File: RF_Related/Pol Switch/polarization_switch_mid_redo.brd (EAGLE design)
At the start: 88.4 x 54.4 mm, 61 parts, among them IC1 VLPR-24-858-2, IC10 ADP-2-1+_MINICIRCUITS, IC11 ADP-2-1+_MINICIRCUITS, IC12 QCV-151+, IC13 MAX8878EUK28+T, IC14 SN74LVC2G17DBVT, IC15 SN74LVC2G17DBVT, IC2 VLPR-24-858-2, IC3 HSWA2-30DR+, IC4 VLPR-24-858-2, IC5 HSWA2-30DR+, IC6 HSWA2-30DR+, IC7 HSWA2-30DR+, IC8 PHA-13LN+, IC9 PHA-13LN+, J1 M20-9730645, J2 171856-0002, X3 SMA-142-0701-801/806, X4 SMA-142-0701-801/806, X5 SMA-142-0701-801/806

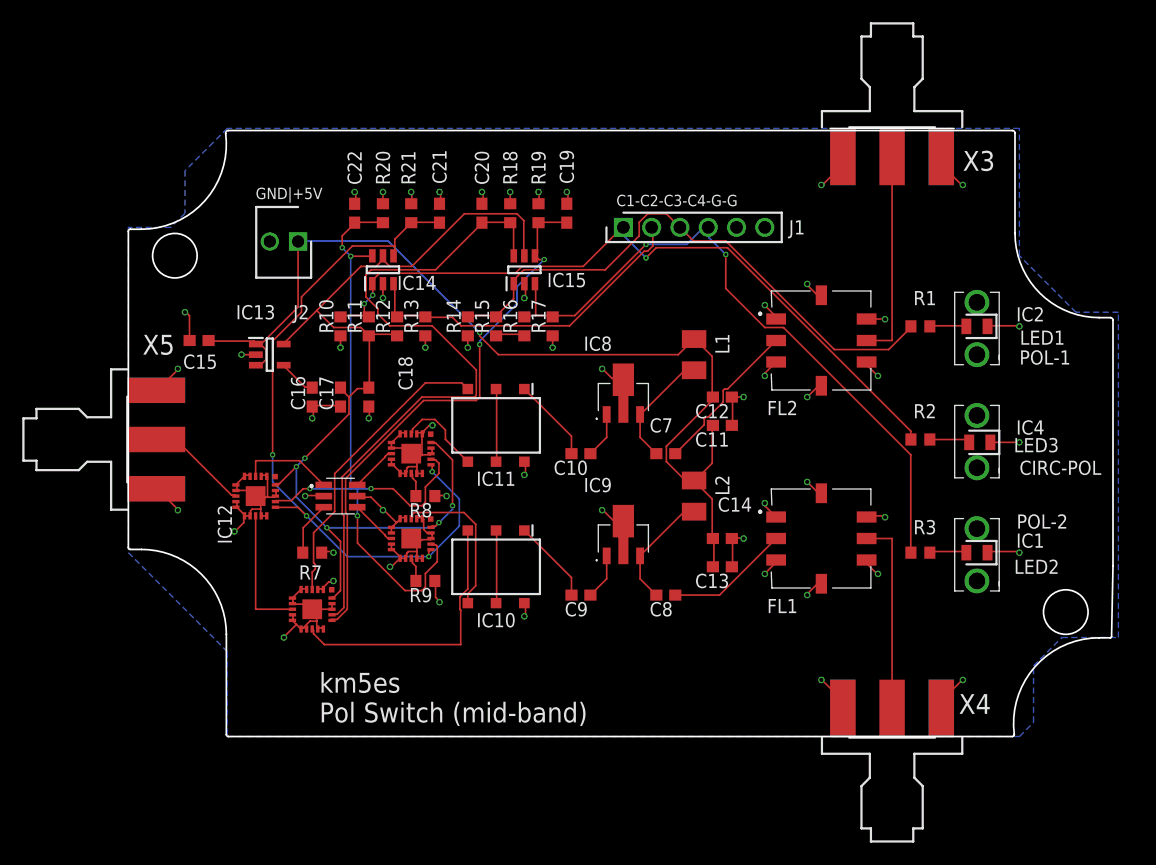
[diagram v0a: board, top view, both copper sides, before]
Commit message: made a new pol switch board with jumper pads. do I need that resistor row? backing up now
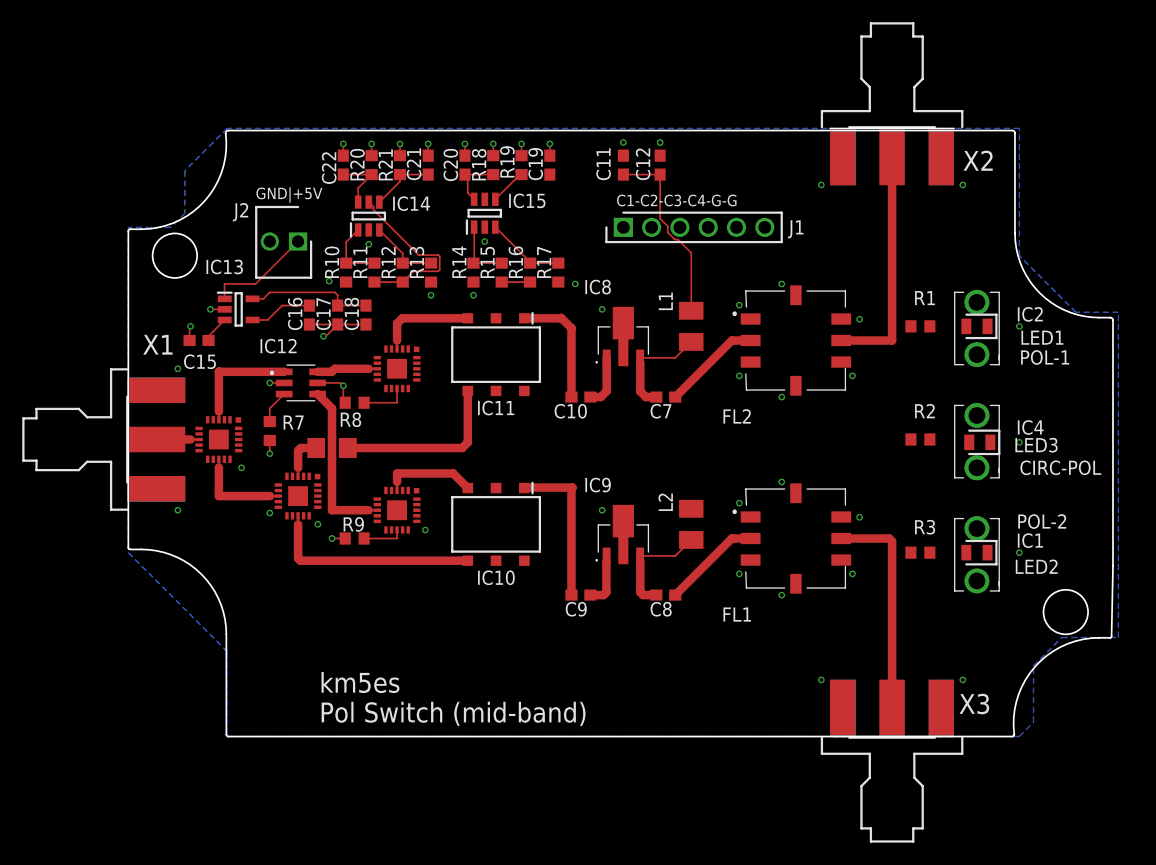
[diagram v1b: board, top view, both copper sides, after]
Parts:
- removed C13: 10e-6, rcl:C0603
- removed C14: 1e-9, rcl:C0603
- removed X4: SMA-142-0701-801/806, sma-flange_375mils:J502-ND-142-0701-801/806
- added R4: 0, rcl:R1206
- added X2: SMA-142-0701-801/806, sma-flange_375mils:J502-ND-142-0701-801/806
- moved X3 54.6 mm to (68.6, 0.00), turned to 90 degrees
- moved C11 25.0 mm to (44.5, 51.3), turned to 270 degrees
- moved C12 21.6 mm to (47.8, 51.3), turned to 270 degrees
- moved R7 11.6 mm to (12.7, 27.4), turned to 90 degrees
- moved IC12 10.8 mm to (15.5, 31.8)
- moved R8 10.5 mm to (20.3, 30.0), turned to 0 degrees
- moved IC5 10.2 mm to (15.2, 21.6)
- moved IC6 7.73 mm to (24.1, 33.0)
- moved R9 7.41 mm to (20.3, 17.8), turned to 0 degrees
- moved C16 7.37 mm to (16.3, 37.8)
- moved C17 7.37 mm to (18.8, 37.8)
- moved C18 7.37 mm to (21.3, 37.8)
- moved IC11 6.35 mm to (33.0, 34.3)
- moved IC15 6.20 mm to (32.0, 47.0)
- moved IC3 6.06 mm to (8.13, 26.7)
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- renumbered X5 to X1
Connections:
- removed net N$18: IC11.4, IC6.3
- removed net N$23: IC11.3, IC5.3
- new net N$10: IC11.4, R4.2
- new net N$11: IC11.3, IC6.3
- new net N$12: IC5.3, R4.1
- net GND: now also X2.G@1, X2.G@2, X2.G@3, X2.G@4; no longer C13.1, C14.1, X4.G@1, X4.G@2, X4.G@3, X4.G@4
- net N$29: now also X2.1; no longer X3.1
- net N$31: now also X3.1; no longer X4.1
- net N$36: no longer C13.2, C14.2
- net N$4: now also IC10.4; no longer IC10.3
- net N$7: now also IC10.3; no longer IC10.4
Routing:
- net GND: track 169.4 -> 25.5 mm, vias 55 -> 50
- net N$39: track 91.6 -> 27.5 mm, vias 5 -> 0
- net N$36: track 90.1 -> 28.8 mm, vias 1 -> 0
- net N$42: track 66.4 -> 5.51 mm, vias 5 -> 0
- net N$37: track 66.5 -> 5.97 mm, vias 3 -> 0
- net N$46: track 65.3 -> 5.78 mm, vias 4 -> 0
- net N$8: track 63.5 -> 5.00 mm
- net N$45: track 60.6 -> 7.06 mm, vias 2 -> 0
- net N$38: track 50.1 -> 3.27 mm, vias 2 -> 0
- net N$44: track 51.5 -> 5.80 mm
- net N$23: track 26.9 -> 0.00 mm
- net N$43: track 31.3 -> 6.39 mm
- net N$10: track 0.00 -> 15.6 mm
- net N$9: track 4.26 -> 15.0 mm
- net N$11: track 0.00 -> 8.83 mm
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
